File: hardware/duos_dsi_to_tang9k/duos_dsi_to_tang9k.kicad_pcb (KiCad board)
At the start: 2 copper layers, 50 x 40 mm, 6 parts, among them J1 Duo_S_DSI_IN, J2 Tang_Nano_9K

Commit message: Use real Duo S CON26A MIPI_TX pinout in DSI adapter project
Co-Authored-By: Claude Sonnet 5.5 <noreply@anthropic.com>
Claude-Session: https://claude.ai/code/session_01Kmp7iiQhgLgwfNawdP6KaV
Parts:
- J1: value Duo_S_DSI_IN -> CON26A_Duo_S; footprint Connector_PinHeader_2.54mm:PinHeader_1x10_P2.54mm_Vertical -> Connector_PinHeader_2.54mm:PinHeader_2x13_P2.54mm_Vertical
- moved J1 4.00 mm to (5.00, 4.50)
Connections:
- J1 pad 1: GND -> DSI_D0_P
- J1 pad 10: GND -> DSI_D2_N
- J1 pad 2: DSI_D0_N -> DSI_D1_P
- J1 pad 3: DSI_D0_P -> DSI_D0_N
- J1 pad 4: GND -> DSI_D1_N
- J1 pad 5: DSI_CK_N -> GND
- J1 pad 6: DSI_CK_P -> GND
- J1 pad 7: GND -> DSI_CK_P
- J1 pad 8: DSI_D1_N -> DSI_D2_P
- J1 pad 9: DSI_D1_P -> DSI_CK_N
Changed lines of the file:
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@@
 (net 6 "DSI_D1_N")
 (net 7 "DSI_D1_P")
-(net 8 "LP_D0P")
-(footprint "Connector_PinHeader_2.54mm:PinHeader_1x10_P2.54mm_Vertical" (layer "F.Cu") (at 5 8.5)
+(net 8 "DSI_D2_N")
+(net 9 "DSI_D2_P")
+(net 10 "DSI_D3_N")
+(net 11 "DSI_D3_P")
+(net 12 "LP_D0P")
+(footprint "Connector_PinHeader_2.54mm:PinHeader_2x13_P2.54mm_Vertical" (layer "F.Cu") (at 5 4.5)
 (property "Reference" "J1" (at 0 -2.5 0) (layer "F.SilkS") (effects (font (size 1.27 1.27))))
-(property "Value" "Duo_S_DSI_IN" (at 0 25.90 0) (layer "F.Fab") (effects (font (size 1.27 1.27))))
-(fp_rect (start -1.33 -1.33) (end 1.33 24.19) (stroke (width 0.12) (type default)) (fill none) (layer "F.SilkS"))
-(pad "1" thru_hole rect (at 0 0.00) (size 1.7 1.7) (drill 1.0) (layers "*.Cu" "*.Mask") (net 1 "GND"))
-(pad "2" thru_hole oval (at 0 2.54) (size 1.7 1.7) (drill 1.0) (layers "*.Cu" "*.Mask") (net 4 "DSI_D0_N"))
-(pad "3" thru_hole oval (at 0 5.08) (size 1.7 1.7) (drill 1.0) (layers "*.Cu" "*.Mask") (net 5 "DSI_D0_P"))
-(pad "4" thru_hole oval (at 0 7.62) (size 1.7 1.7) (drill 1.0) (layers "*.Cu" "*.Mask") (net 1 "GND"))
-(pad "5" thru_hole oval (at 0 10.16) (size 1.7 1.7) (drill 1.0) (layers "*.Cu" "*.Mask") (net 2 "DSI_CK_N"))
-(pad "6" thru_hole oval (at 0 12.70) (size 1.7 1.7) (drill 1.0) (layers "*.Cu" "*.Mask") (net 3 "DSI_CK_P"))
-(pad "7" thru_hole oval (at 0 15.24) (size 1.7 1.7) (drill 1.0) (layers "*.Cu" "*.Mask") (net 1 "GND"))
-(pad "8" thru_hole oval (at 0 17.78) (size 1.7 1.7) (drill 1.0) (layers "*.Cu" "*.Mask") (net 6 "DSI_D1_N"))
-(pad "9" thru_hole oval (at 0 20.32) (size 1.7 1.7) (drill 1.0) (layers "*.Cu" "*.Mask") (net 7 "DSI_D1_P"))
-(pad "10" thru_hole oval (at 0 22.86) (size 1.7 1.7) (drill 1.0) (layers "*.Cu" "*.Mask") (net 1 "GND"))
+(property "Value" "CON26A_Duo_S" (at 0 33.52 0) (layer "F.Fab") (effects (font (size 1.27 1.27))))
+(fp_rect (start -1.33 -1.33) (end 3.87 31.81) (stroke (width 0.12) (type default)) (fill none) (layer "F.SilkS"))
+(pad "1" thru_hole rect (at 0.00 0.00) (size 1.7 1.7) (drill 1.0) (layers "*.Cu" "*.Mask") (net 5 "DSI_D0_P"))
+(pad "2" thru_hole oval (at 2.54 0.00) (size 1.7 1.7) (drill 1.0) (layers "*.Cu" "*.Mask") (net 7 "DSI_D1_P"))
+(pad "3" thru_hole oval (at 0.00 2.54) (size 1.7 1.7) (drill 1.0) (layers "*.Cu" "*.Mask") (net 4 "DSI_D0_N"))
+(pad "4" thru_hole oval (at 2.54 2.54) (size 1.7 1.7) (drill 1.0) (layers "*.Cu" "*.Mask") (net 6 "DSI_D1_N"))
+(pad "5" thru_hole oval (at 0.00 5.08) (size 1.7 1.7) (drill 1.0) (layers "*.Cu" "*.Mask") (net 1 "GND"))
+(pad "6" thru_hole oval (at 2.54 5.08) (size 1.7 1.7) (drill 1.0) (layers "*.Cu" "*.Mask") (net 1 "GND"))
+(pad "7" thru_hole oval (at 0.00 7.62) (size 1.7 1.7) (drill 1.0) (layers "*.Cu" "*.Mask") (net 3 "DSI_CK_P"))
+(pad "8" thru_hole oval (at 2.54 7.62) (size 1.7 1.7) (drill 1.0) (layers "*.Cu" "*.Mask") (net 9 "DSI_D2_P"))
+(pad "9" thru_hole oval (at 0.00 10.16) (size 1.7 1.7) (drill 1.0) (layers "*.Cu" "*.Mask") (net 2 "DSI_CK_N"))
+(pad "10" thru_hole oval (at 2.54 10.16) (size 1.7 1.7) (drill 1.0) (layers "*.Cu" "*.Mask") (net 8 "DSI_D2_N"))
+(pad "11" thru_hole oval (at 0.00 12.70) (size 1.7 1.7) (drill 1.0) (layers "*.Cu" "*.Mask") (net 1 "GND"))
+(pad "12" thru_hole oval (at 2.54 12.70) (size 1.7 1.7) (drill 1.0) (layers "*.Cu" "*.Mask") (net 1 "GND"))
+(pad "13" thru_hole oval (at 0.00 15.24) (size 1.7 1.7) (drill 1.0) (layers "*.Cu" "*.Mask") (net 11 "DSI_D3_P"))
+(pad "14" thru_hole oval (at 2.54 15.24) (size 1.7 1.7) (drill 1.0) (layers "*.Cu" "*.Mask"))
+(pad "15" thru_hole oval (at 0.00 17.78) (size 1.7 1.7) (drill 1.0) (layers "*.Cu" "*.Mask") (net 10 "DSI_D3_N"))
+(pad "16" thru_hole oval (at 2.54 17.78) (size 1.7 1.7) (drill 1.0) (layers "*.Cu" "*.Mask"))
+(pad "17" thru_hole oval (at 0.00 20.32) (size 1.7 1.7) (drill 1.0) (layers "*.Cu" "*.Mask"))
+(pad "18" thru_hole oval (at 2.54 20.32) (size 1.7 1.7) (drill 1.0) (layers "*.Cu" "*.Mask"))
+(pad "19" thru_hole oval (at 0.00 22.86) (size 1.7 1.7) (drill 1.0) (layers "*.Cu" "*.Mask"))
+(pad "20" thru_hole oval (at 2.54 22.86) (size 1.7 1.7) (drill 1.0) (layers "*.Cu" "*.Mask"))
+(pad "21" thru_hole oval (at 0.00 25.40) (size 1.7 1.7) (drill 1.0) (layers "*.Cu" "*.Mask"))
+(pad "22" thru_hole oval (at 2.54 25.40) (size 1.7 1.7) (drill 1.0) (layers "*.Cu" "*.Mask"))
+(pad "23" thru_hole oval (at 0.00 27.94) (size 1.7 1.7) (drill 1.0) (layers "*.Cu" "*.Mask"))
+(pad "24" thru_hole oval (at 2.54 27.94) (size 1.7 1.7) (drill 1.0) (layers "*.Cu" "*.Mask"))
+(pad "25" thru_hole oval (at 0.00 30.48) (size 1.7 1.7) (drill 1.0) (layers "*.Cu" "*.Mask"))
+(pad "26" thru_hole oval (at 2.54 30.48) (size 1.7 1.7) (drill 1.0) (layers "*.Cu" "*.Mask"))
 )
 (footprint "Connector_PinHeader_2.54mm:PinHeader_1x08_P2.54mm_Vertical" (layer "F.Cu") (at 45 11)
@@
 (property "Value" "Tang_Nano_9K" (at 0 20.82 0) (layer "F.Fab") (effects (font (size 1.27 1.27))))
 (fp_rect (start -1.33 -1.33) (end 1.33 19.11) (stroke (width 0.12) (type default)) (fill none) (layer "F.SilkS"))
-(pad "1" thru_hole rect (at 0 0.00) (size 1.7 1.7) (drill 1.0) (layers "*.Cu" "*.Mask") (net 3 "DSI_CK_P"))
-(pad "2" thru_hole oval (at 0 2.54) (size 1.7 1.7) (drill 1.0) (layers "*.Cu" "*.Mask") (net 2 "DSI_CK_N"))
-(pad "3" thru_hole oval (at 0 5.08) (size 1.7 1.7) (drill 1.0) (layers "*.Cu" "*.Mask") (net 5 "DSI_D0_P"))
-(pad "4" thru_hole oval (at 0 7.62) (size 1.7 1.7) (drill 1.0) (layers "*.Cu" "*.Mask") (net 4 "DSI_D0_N"))
-(pad "5" thru_hole oval (at 0 10.16) (size 1.7 1.7) (drill 1.0) (layers "*.Cu" "*.Mask") (net 7 "DSI_D1_P"))
-(pad "6" thru_hole oval (at 0 12.70) (size 1.7 1.7) (drill 1.0) (layers "*.Cu" "*.Mask") (net 6 "DSI_D1_N"))
-(pad "7" thru_hole oval (at 0 15.24) (size 1.7 1.7) (drill 1.0) (layers "*.Cu" "*.Mask") (net 8 "LP_D0P"))
-(pad "8" thru_hole oval (at 0 17.78) (size 1.7 1.7) (drill 1.0) (layers "*.Cu" "*.Mask") (net 1 "GND"))
+(pad "1" thru_hole rect (at 0.00 0.00) (size 1.7 1.7) (drill 1.0) (layers "*.Cu" "*.Mask") (net 3 "DSI_CK_P"))
+(pad "2" thru_hole oval (at 0.00 2.54) (size 1.7 1.7) (drill 1.0) (layers "*.Cu" "*.Mask") (net 2 "DSI_CK_N"))
+(pad "3" thru_hole oval (at 0.00 5.08) (size 1.7 1.7) (drill 1.0) (layers "*.Cu" "*.Mask") (net 5 "DSI_D0_P"))
+(pad "4" thru_hole oval (at 0.00 7.62) (size 1.7 1.7) (drill 1.0) (layers "*.Cu" "*.Mask") (net 4 "DSI_D0_N"))
+(pad "5" thru_hole oval (at 0.00 10.16) (size 1.7 1.7) (drill 1.0) (layers "*.Cu" "*.Mask") (net 7 "DSI_D1_P"))
+(pad "6" thru_hole oval (at 0.00 12.70) (size 1.7 1.7) (drill 1.0) (layers "*.Cu" "*.Mask") (net 6 "DSI_D1_N"))
+(pad "7" thru_hole oval (at 0.00 15.24) (size 1.7 1.7) (drill 1.0) (layers "*.Cu" "*.Mask") (net 12 "LP_D0P"))
+(pad "8" thru_hole oval (at 0.00 17.78) (size 1.7 1.7) (drill 1.0) (layers "*.Cu" "*.Mask") (net 1 "GND"))
 )
 (footprint "Resistor_SMD:R_0402_1005Metric" (layer "F.Cu") (at 30 10 90)
@@
 (property "Value" "470R" (at 0 1.2 90) (layer "F.Fab") (effects (font (size 1.27 1.27))))
 (pad "1" smd roundrect (at -0.51 0) (size 0.54 0.64) (layers "F.Cu" "F.Paste" "F.Mask") (roundrect_rratio 0.25) (net 5 "DSI_D0_P"))
-(pad "2" smd roundrect (at 0.51 0) (size 0.54 0.64) (layers "F.Cu" "F.Paste" "F.Mask") (roundrect_rratio 0.25) (net 8 "LP_D0P"))
+(pad "2" smd roundrect (at 0.51 0) (size 0.54 0.64) (layers "F.Cu" "F.Paste" "F.Mask") (roundrect_rratio 0.25) (net 12 "LP_D0P"))
 )
 (gr_rect (start 0 0) (end 50 40) (stroke (width 0.1) (type default)) (fill none) (layer "Edge.Cuts"))

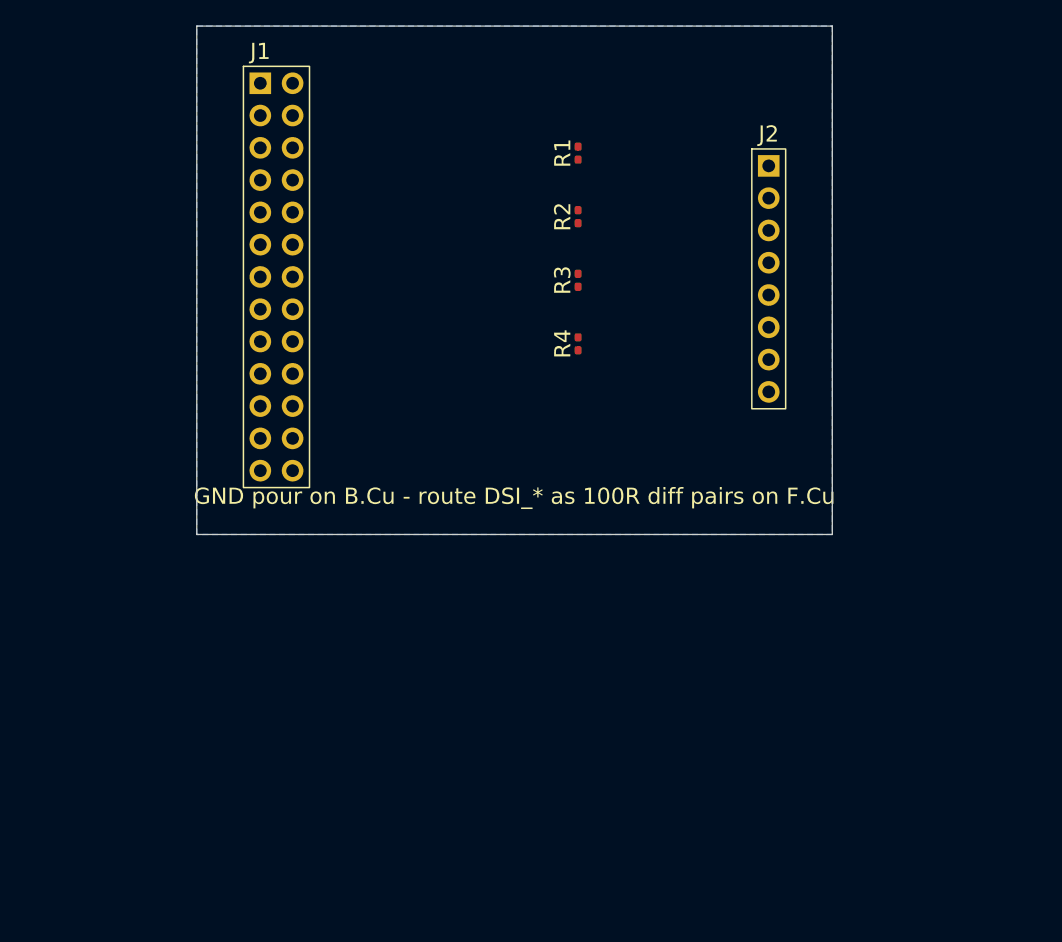
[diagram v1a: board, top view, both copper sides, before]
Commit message: DSI adapter: Tang header pinout, split termination, LP level shifters on pins 25/26
Co-Authored-By: Claude Sonnet 5.5 <noreply@anthropic.com>
Claude-Session: https://claude.ai/code/session_01Kmp7iiQhgLgwfNawdP6KaV
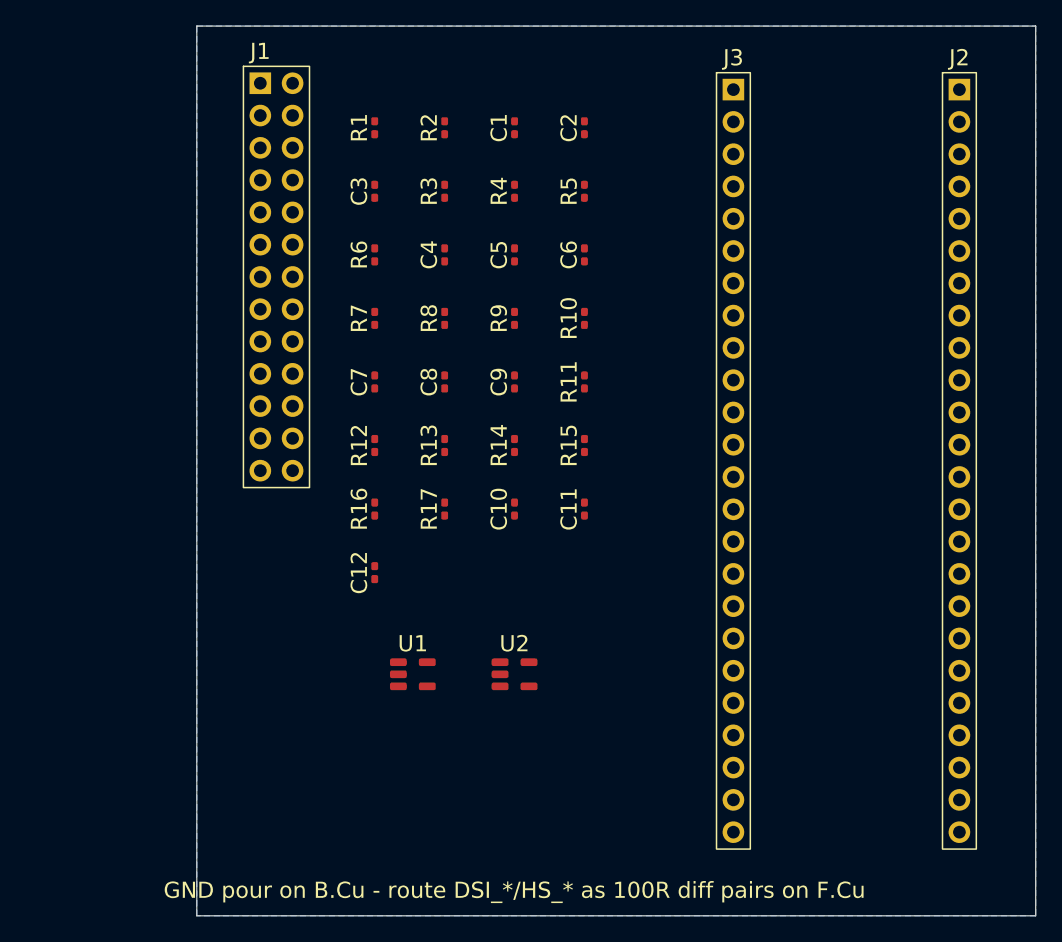
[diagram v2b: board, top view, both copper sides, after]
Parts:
- added C1: 100nF, Capacitor_SMD:C_0402_1005Metric, F.Cu at (25.0, 8.00)
- added C10: 100nF, Capacitor_SMD:C_0402_1005Metric, F.Cu at (25.0, 38.0)
- added C11: 100nF, Capacitor_SMD:C_0402_1005Metric, F.Cu at (30.5, 38.0)
- added C12: 100nF, Capacitor_SMD:C_0402_1005Metric, F.Cu at (14.0, 43.0)
- added C2: 100nF, Capacitor_SMD:C_0402_1005Metric, F.Cu at (30.5, 8.00)
- added C3: 100nF, Capacitor_SMD:C_0402_1005Metric, F.Cu at (14.0, 13.0)
- added C4: 100nF, Capacitor_SMD:C_0402_1005Metric, F.Cu at (19.5, 18.0)
- added C5: 100nF, Capacitor_SMD:C_0402_1005Metric, F.Cu at (25.0, 18.0)
- added C6: 100nF, Capacitor_SMD:C_0402_1005Metric, F.Cu at (30.5, 18.0)
- added C7: 100nF, Capacitor_SMD:C_0402_1005Metric, F.Cu at (14.0, 28.0)
- added C8: 100nF, Capacitor_SMD:C_0402_1005Metric, F.Cu at (19.5, 28.0)
- added C9: 100nF, Capacitor_SMD:C_0402_1005Metric, F.Cu at (25.0, 28.0)
- added J3: Tang_J5, Connector_PinHeader_2.54mm:PinHeader_1x24_P2.54mm_Vertical, F.Cu at (42.2, 5.00)
- added R10: 50R, Resistor_SMD:R_0402_1005Metric, F.Cu at (30.5, 23.0)
- added R11: 10k, Resistor_SMD:R_0402_1005Metric, F.Cu at (30.5, 28.0)
- added R12: 10k, Resistor_SMD:R_0402_1005Metric, F.Cu at (14.0, 33.0)
- added R13: 470R, Resistor_SMD:R_0402_1005Metric, F.Cu at (19.5, 33.0)
- added R14: 470R, Resistor_SMD:R_0402_1005Metric, F.Cu at (25.0, 33.0)
- added R15: 470R, Resistor_SMD:R_0402_1005Metric, F.Cu at (30.5, 33.0)
- added R16: 27k, Resistor_SMD:R_0402_1005Metric, F.Cu at (14.0, 38.0)
- added R17: 10k, Resistor_SMD:R_0402_1005Metric, F.Cu at (19.5, 38.0)
- added R5: 50R, Resistor_SMD:R_0402_1005Metric, F.Cu at (30.5, 13.0)
- added R6: 50R, Resistor_SMD:R_0402_1005Metric, F.Cu at (14.0, 18.0)
- added R7: 10k, Resistor_SMD:R_0402_1005Metric, F.Cu at (14.0, 23.0)
- added R8: 10k, Resistor_SMD:R_0402_1005Metric, F.Cu at (19.5, 23.0)
- added R9: 50R, Resistor_SMD:R_0402_1005Metric, F.Cu at (25.0, 23.0)
- added U1: SN74AUP1T17, Package_TO_SOT_SMD:SOT-23-5, F.Cu at (17.0, 51.0)
- added U2: SN74AUP1T17, Package_TO_SOT_SMD:SOT-23-5, F.Cu at (25.0, 51.0)
- J2: value Tang_Nano_9K -> Tang_J6; footprint Connector_PinHeader_2.54mm:PinHeader_1x08_P2.54mm_Vertical -> Connector_PinHeader_2.54mm:PinHeader_1x24_P2.54mm_Vertical
- R1, R2: value 100R -> 50R
- R3: value 100R -> 10k
- R4: value 470R -> 10k
- moved J2 16.2 mm to (60.0, 5.00)
- moved R1 16.1 mm to (14.0, 8.00)
- moved R4 13.0 mm to (25.0, 13.0)
- moved R2 12.6 mm to (19.5, 8.00)
- moved R3 12.6 mm to (19.5, 13.0)
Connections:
- J2 pad 1: DSI_CK_P -> (no net)
- J2 pad 2: DSI_CK_N -> (no net)
- J2 pad 3: DSI_D0_P -> LP_D0_P
- J2 pad 4: DSI_D0_N -> HS_D1_P
- J2 pad 5: DSI_D1_P -> HS_D1_N
- J2 pad 6: DSI_D1_N -> HS_D0_P
- J2 pad 7: LP_D0P -> HS_D0_N
- J2 pad 8: GND -> HS_CK_P
- R1 pad 2: DSI_CK_N -> MID_CK
- R2 pad 1: DSI_D0_P -> DSI_CK_N
- R2 pad 2: DSI_D0_N -> MID_CK
- R3 pad 1: DSI_D1_P -> HS_CK_P
- R3 pad 2: DSI_D1_N -> VCM
- R4 pad 1: DSI_D0_P -> HS_CK_N
- R4 pad 2: LP_D0P -> VCM
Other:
- board size 50 x 40 mm -> 66 x 70 mm
- board text added: "GND pour on B.Cu - route DSI_*/HS_* as 100R diff pairs on F.Cu"
- board text removed: "GND pour on B.Cu - route DSI_* as 100R diff pairs on F.Cu"
